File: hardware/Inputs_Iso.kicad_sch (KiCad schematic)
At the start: 41 parts, among them J4 Screw_Terminal_01x02, J5 Screw_Terminal_01x02, J6 Screw_Terminal_01x02, J7 Screw_Terminal_01x02, U3 LTV-847S

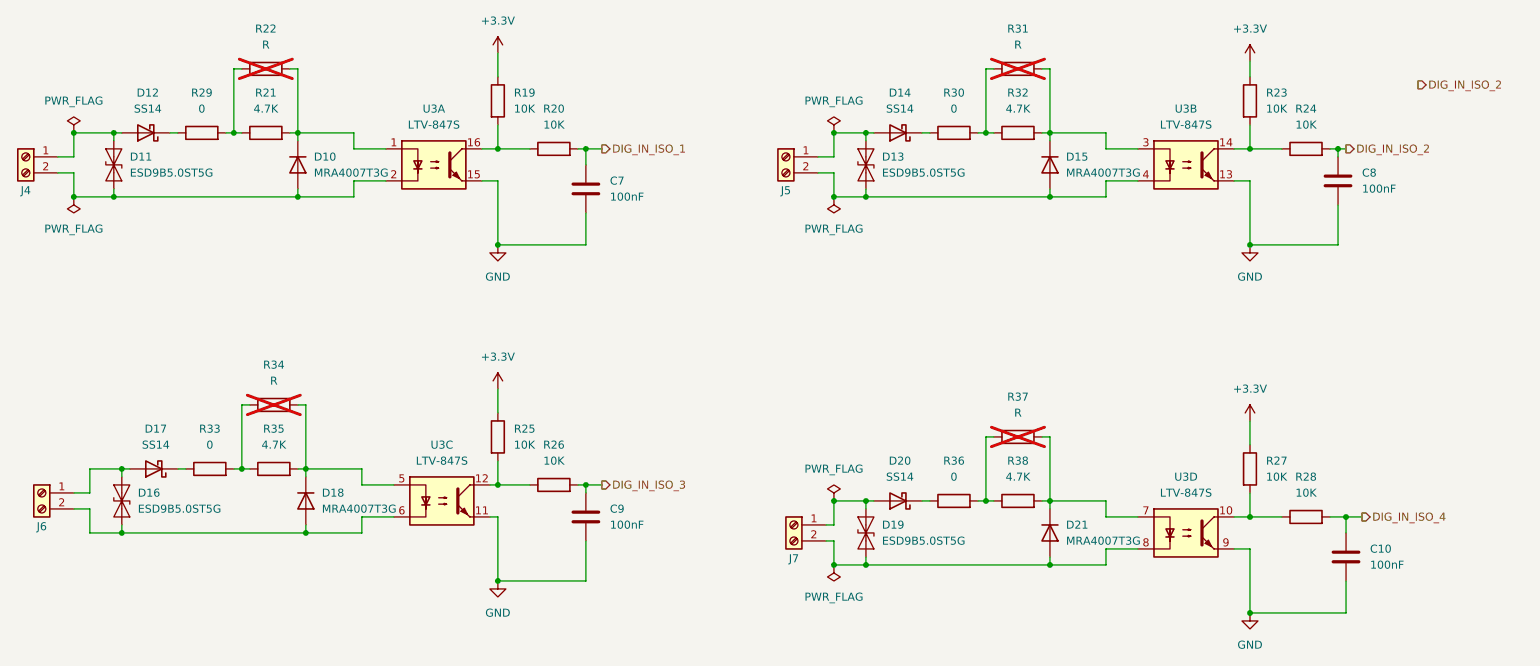
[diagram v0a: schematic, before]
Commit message: Add footprint to components
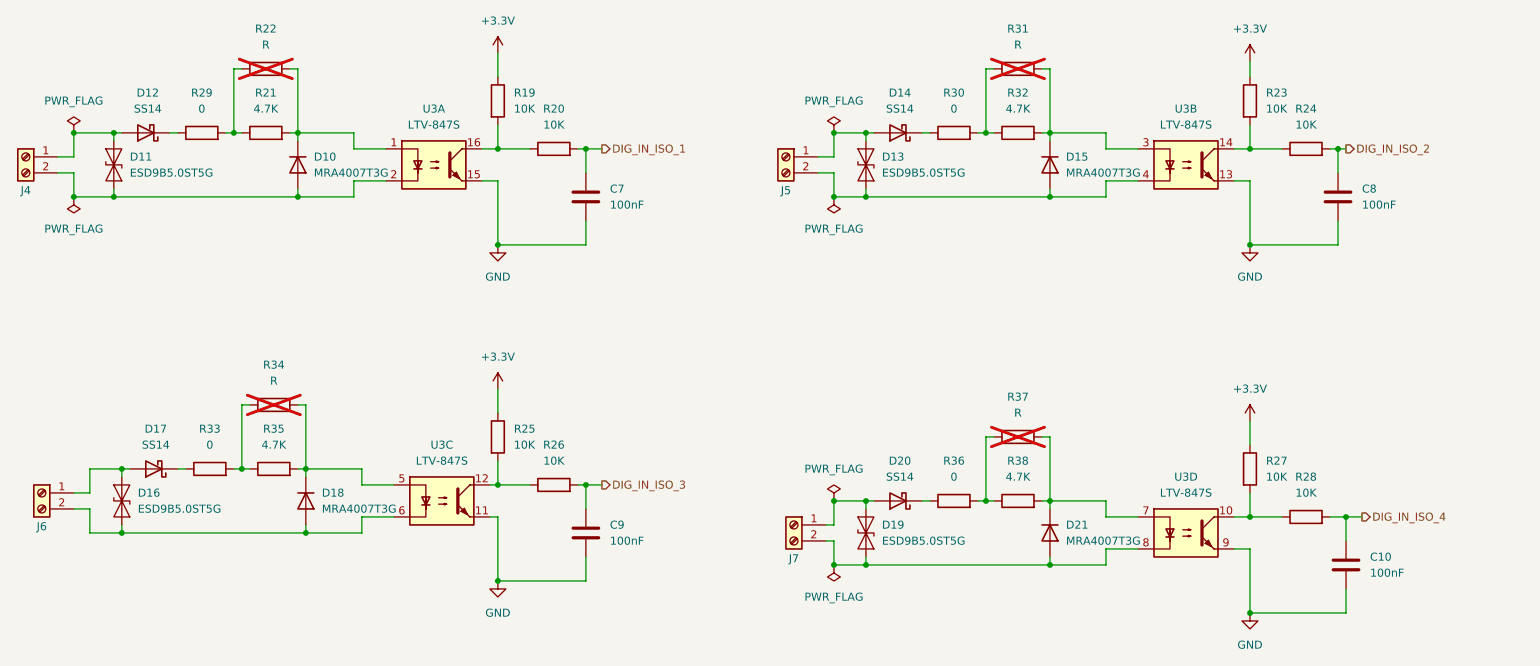
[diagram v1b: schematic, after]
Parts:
- C10, C7, C8, C9: footprint (none) -> Capacitor_SMD:C_0603_1608Metric_Pad1.08x0.95mm_HandSolder
- R19, R20, R21, R22, R23, R24, R25, R26, R27, R28, R29, R30, R31, R32, R33, R35, R36, R37, R38: footprint (none) -> Resistor_SMD:R_0603_1608Metric_Pad0.98x0.95mm_HandSolder
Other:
- moved on the sheet: C10, C7, C8, C9

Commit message: Improvements
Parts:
- J22: renamed from J4; footprint (none) -> TerminalBlock_Phoenix:TerminalBlock_Phoenix_MKDS-1,5-2-5.08_1x02_P5.08mm_Horizontal
- J23: renamed from J6; footprint (none) -> TerminalBlock_Phoenix:TerminalBlock_Phoenix_MKDS-1,5-2-5.08_1x02_P5.08mm_Horizontal
- J24: renamed from J5; footprint (none) -> TerminalBlock_Phoenix:TerminalBlock_Phoenix_MKDS-1,5-2-5.08_1x02_P5.08mm_Horizontal
- J25: renamed from J7; footprint (none) -> TerminalBlock_Phoenix:TerminalBlock_Phoenix_MKDS-1,5-2-5.08_1x02_P5.08mm_Horizontal
- R77: renamed from R34; footprint (none) -> Resistor_SMD:R_0603_1608Metric_Pad0.98x0.95mm_HandSolder
- renumbered C7 to C68, C9 to C69, C8 to C70, C10 to C71, D11 to D38, D16 to D39, D12 to D40, D17 to D41, D10 to D42, D18 to D43, D13 to D44, D19 to D45, D14 to D46, D20 to D47, D15 to D48, D21 to D49, R29 to R73, R33 to R74, R22 to R75, R21 to R76, R35 to R78, R19 to R79, R25 to R80, R20 to R81, R26 to R82, R30 to R83, R36 to R84, R31 to R85, R32 to R86, R37 to R87, R38 to R88, R23 to R89, R27 to R90, R24 to R91, R28 to R92, U3 to U15

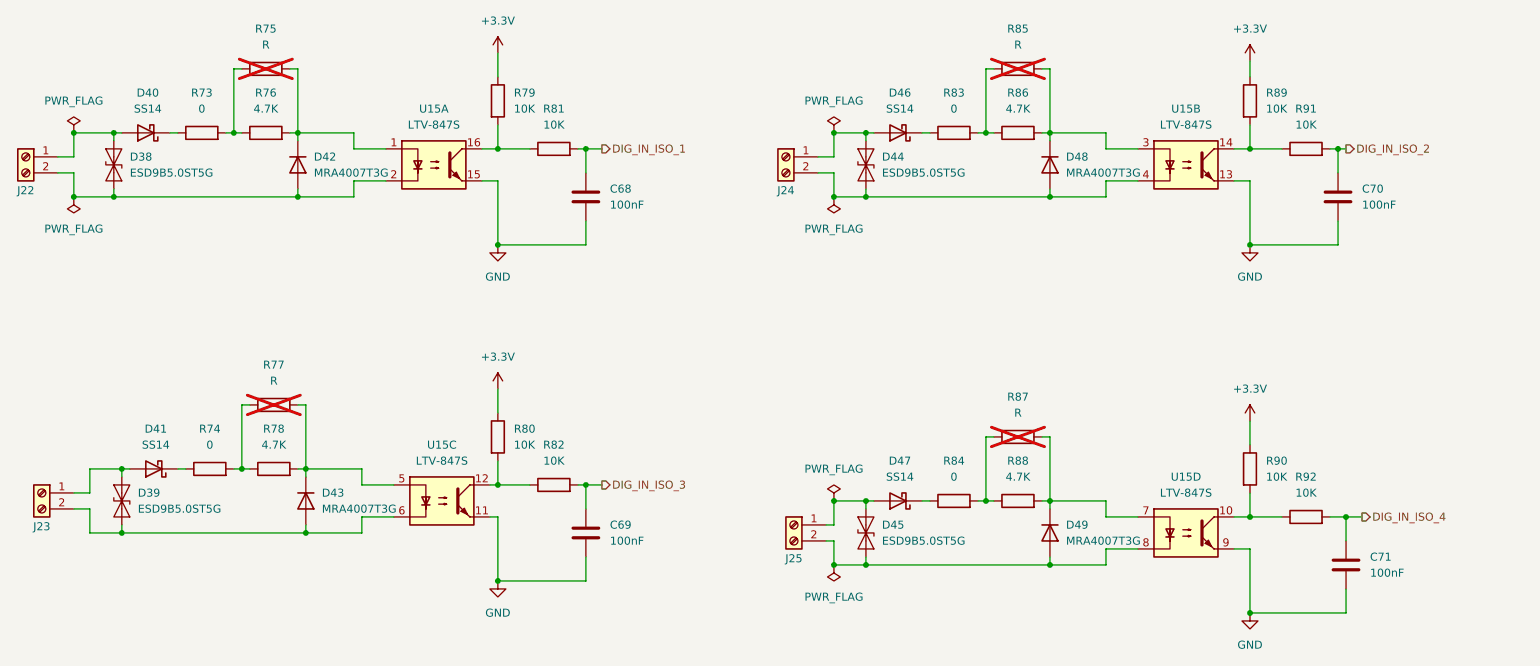
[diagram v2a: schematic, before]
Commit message: Make connectors DB9
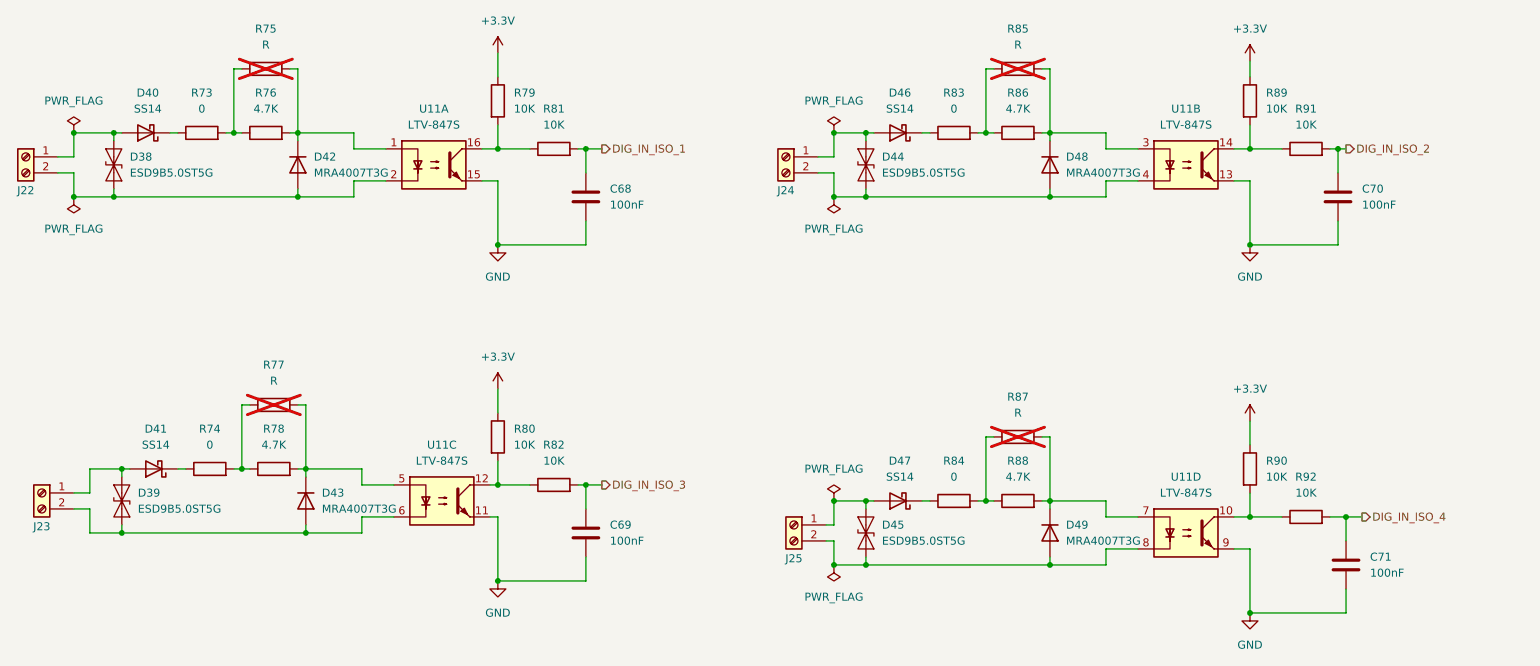
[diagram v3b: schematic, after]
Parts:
- renumbered U15 to U11
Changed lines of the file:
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@@
 		(dnp no)
 		(fields_autoplaced yes)
-		(property "Reference" "#PWR085"
+		(property "Reference" "#PWR089"
 			(at 100.33 39.37 0)
 			(effects
@@
 			(project ""
 				(path "/05707d4e-3d4a-41f6-9822-862f6f3b507e/399015c2-6547-45ba-99d6-e9d0efcd95ce"
-					(reference "#PWR085")
+					(reference "#PWR089")
 					(unit 1)
 				)
@@
 		(dnp no)
 		(fields_autoplaced yes)
-		(property "Reference" "#PWR090"
+		(property "Reference" "#PWR094"
 			(at 219.71 72.39 0)
 			(effects
@@
 			(project "MQTTGateway"
 				(path "/05707d4e-3d4a-41f6-9822-862f6f3b507e/399015c2-6547-45ba-99d6-e9d0efcd95ce"
-					(reference "#PWR090")
+					(reference "#PWR094")
 					(unit 1)
 				)
@@
 		(dnp no)
 		(fields_autoplaced yes)
-		(property "Reference" "U15"
+		(property "Reference" "U11"
 			(at 209.55 102.87 0)
 			(effects
@@
 			(project ""
 				(path "/05707d4e-3d4a-41f6-9822-862f6f3b507e/399015c2-6547-45ba-99d6-e9d0efcd95ce"
-					(reference "U15")
+					(reference "U11")
 					(unit 4)
 				)
@@
 		(dnp no)
 		(fields_autoplaced yes)
-		(property "Reference" "#PWR089"
+		(property "Reference" "#PWR093"
 			(at 219.71 40.64 0)
 			(effects
@@
 			(project "MQTTGateway"
 				(path "/05707d4e-3d4a-41f6-9822-862f6f3b507e/399015c2-6547-45ba-99d6-e9d0efcd95ce"
-					(reference "#PWR089")
+					(reference "#PWR093")
 					(unit 1)
 				)
@@
 		(dnp no)
 		(fields_autoplaced yes)
-		(property "Reference" "#PWR088"
+		(property "Reference" "#PWR092"
 			(at 100.33 125.73 0)
 			(effects
@@
 			(project "MQTTGateway"
 				(path "/05707d4e-3d4a-41f6-9822-862f6f3b507e/399015c2-6547-45ba-99d6-e9d0efcd95ce"
-					(reference "#PWR088")
+					(reference "#PWR092")
 					(unit 1)
 				)
@@
 		(dnp no)
 		(fields_autoplaced yes)
-		(property "Reference" "#PWR087"
+		(property "Reference" "#PWR091"
 			(at 100.33 92.71 0)
 			(effects
@@
 			(project "MQTTGateway"
 				(path "/05707d4e-3d4a-41f6-9822-862f6f3b507e/399015c2-6547-45ba-99d6-e9d0efcd95ce"
-					(reference "#PWR087")
+					(reference "#PWR091")
 					(unit 1)
 				)
@@
 		(dnp no)
 		(fields_autoplaced yes)
-		(property "Reference" "U15"
+		(property "Reference" "U11"
 			(at 209.55 44.45 0)
 			(effects
@@
 			(project ""
 				(path "/05707d4e-3d4a-41f6-9822-862f6f3b507e/399015c2-6547-45ba-99d6-e9d0efcd95ce"
-					(reference "U15")
+					(reference "U11")
 					(unit 2)
 				)
@@
 		(dnp no)
 		(fields_autoplaced yes)
-		(property "Reference" "U15"
+		(property "Reference" "U11"
 			(at 91.44 97.79 0)
 			(effects
@@
 			(project ""
 				(path "/05707d4e-3d4a-41f6-9822-862f6f3b507e/399015c2-6547-45ba-99d6-e9d0efcd95ce"
-					(reference "U15")
+					(reference "U11")
 					(unit 3)
 				)
@@
 		(dnp no)
 		(fields_autoplaced yes)
-		(property "Reference" "#PWR086"
+		(property "Reference" "#PWR090"
 			(at 100.33 72.39 0)
 			(effects
@@
 			(project ""
 				(path "/05707d4e-3d4a-41f6-9822-862f6f3b507e/399015c2-6547-45ba-99d6-e9d0efcd95ce"
-					(reference "#PWR086")
+					(reference "#PWR090")
 					(unit 1)
 				)
@@
 		(dnp no)
 		(fields_autoplaced yes)
-		(property "Reference" "U15"
+		(property "Reference" "U11"
 			(at 90.17 44.45 0)
 			(effects
@@
 			(project ""
 				(path "/05707d4e-3d4a-41f6-9822-862f6f3b507e/399015c2-6547-45ba-99d6-e9d0efcd95ce"
-					(reference "U15")
+					(reference "U11")
 					(unit 1)
 				)
@@
 		(dnp no)
 		(fields_autoplaced yes)
-		(property "Reference" "#PWR091"
+		(property "Reference" "#PWR095"
 			(at 219.71 97.79 0)
 			(effects
@@
 			(project "MQTTGateway"
 				(path "/05707d4e-3d4a-41f6-9822-862f6f3b507e/399015c2-6547-45ba-99d6-e9d0efcd95ce"
-					(reference "#PWR091")
+					(reference "#PWR095")
 					(unit 1)
 				)
@@
 		(dnp no)
 		(fields_autoplaced yes)
-		(property "Reference" "#PWR092"
+		(property "Reference" "#PWR096"
 			(at 219.71 130.81 0)
 			(effects
@@
 			(project "MQTTGateway"
 				(path "/05707d4e-3d4a-41f6-9822-862f6f3b507e/399015c2-6547-45ba-99d6-e9d0efcd95ce"
-					(reference "#PWR092")
+					(reference "#PWR096")
 					(unit 1)
 				)
